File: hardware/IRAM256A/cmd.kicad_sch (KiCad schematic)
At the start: 32 parts

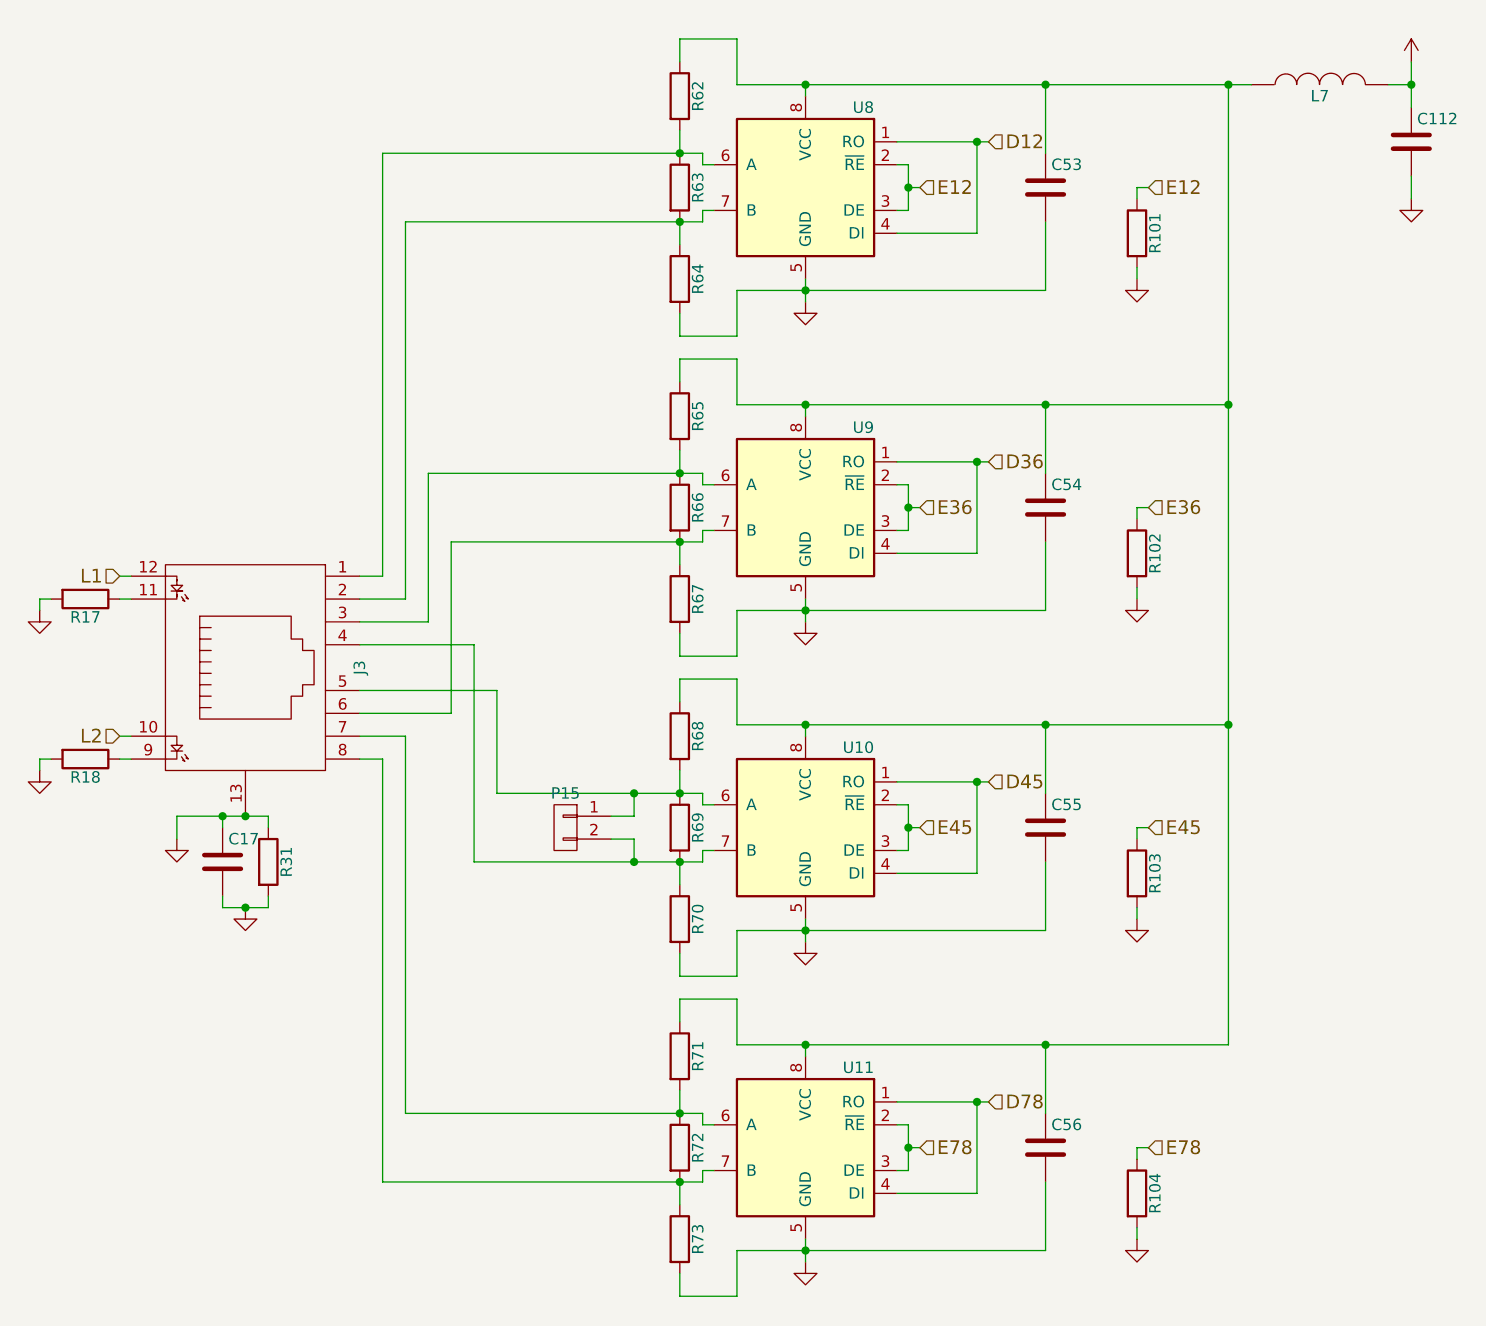
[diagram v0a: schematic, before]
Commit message: Structure change + kicad 3d models updated
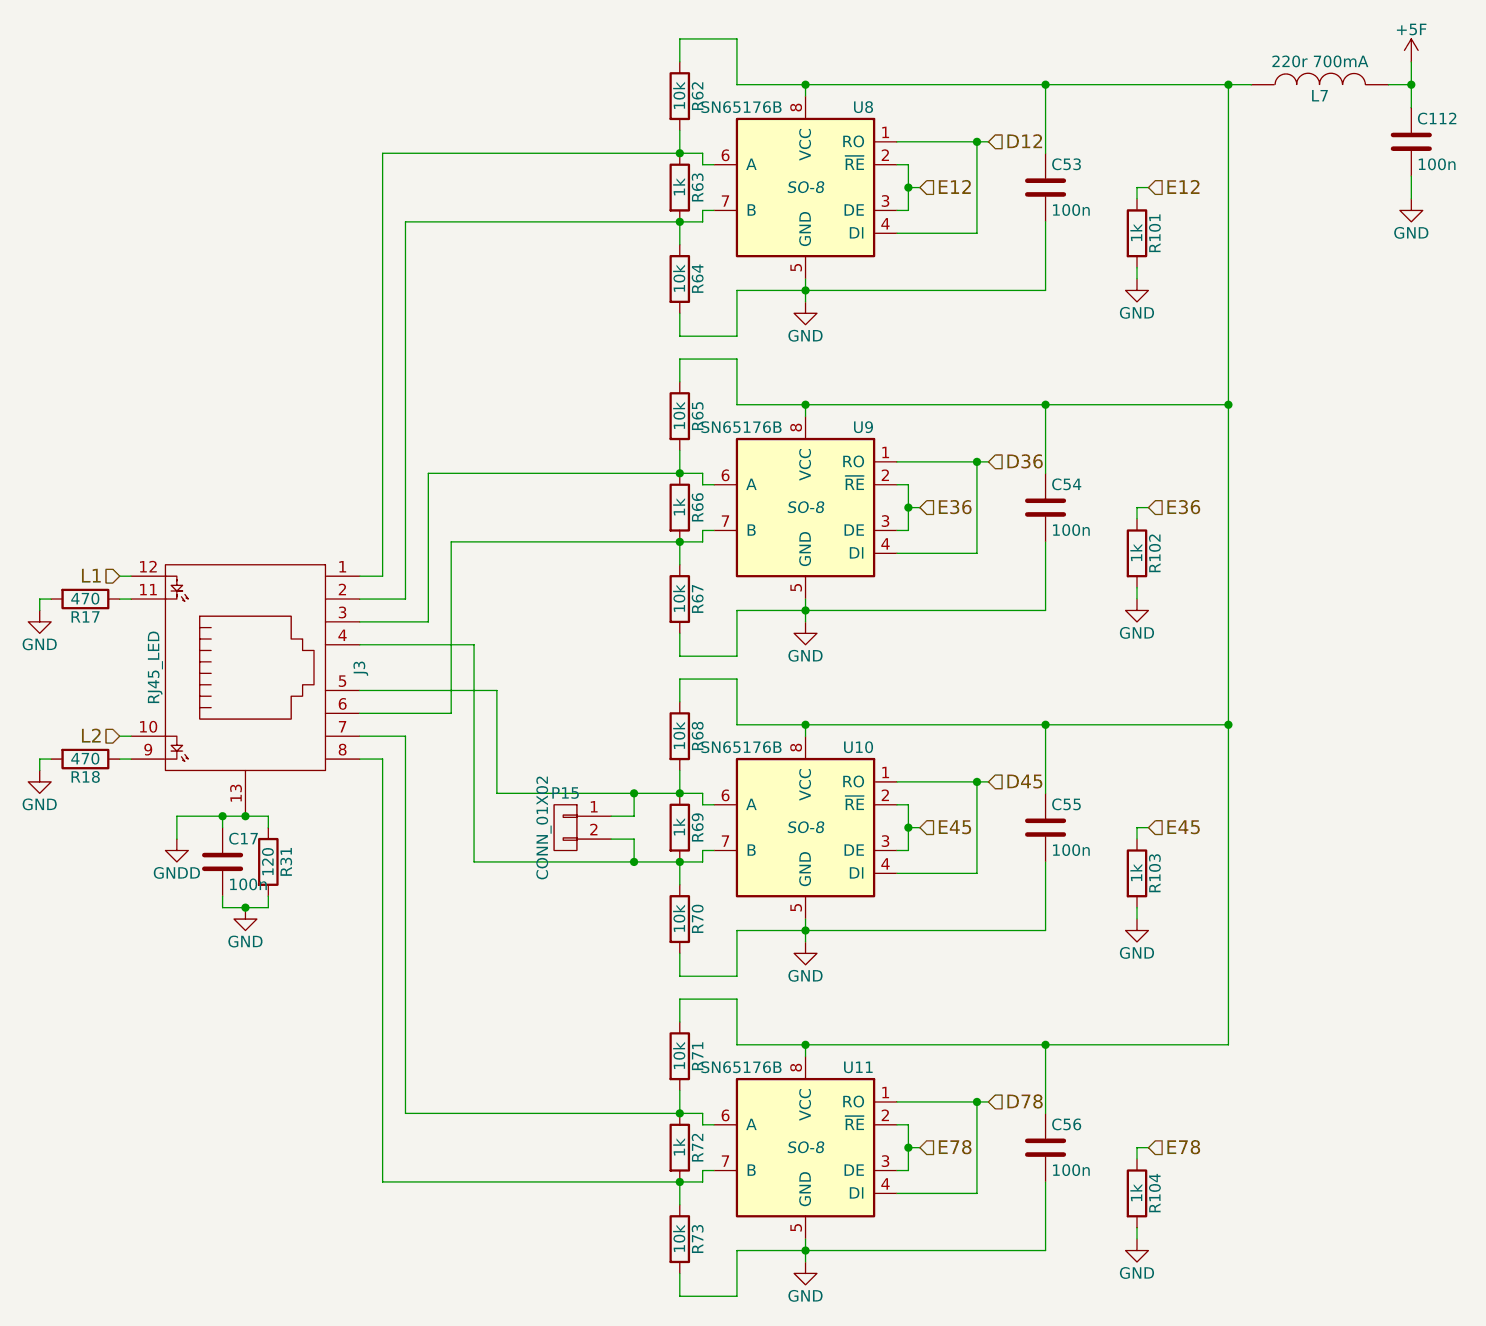
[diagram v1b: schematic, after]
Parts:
- C112, C17, C53, C54, C55, C56: value (none) -> 100n; footprint (none) -> stmbl:C_0603
- J3: value (none) -> RJ45_LED; footprint (none) -> stmbl:RJ45_LED
- L7: value (none) -> 220r 700mA; footprint (none) -> stmbl:R_0603
- P15: value (none) -> CONN_01X02; footprint (none) -> stmbl:RM3.5_1x2
- R101, R102, R103, R104, R63, R66, R69, R72: value (none) -> 1k; footprint (none) -> stmbl:R_0603
- R17, R18: value (none) -> 470; footprint (none) -> stmbl:R_0603
- R31: value (none) -> 120; footprint (none) -> stmbl:R_0603
- R62, R64, R65, R67, R68, R70, R71, R73: value (none) -> 10k; footprint (none) -> stmbl:R_0603
- U10, U11, U8, U9: value (none) -> SN65176B; footprint (none) -> SO-8
